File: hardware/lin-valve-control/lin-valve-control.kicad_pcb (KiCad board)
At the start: 4 copper layers, 55.6 x 43.2 mm, 46 parts, among them J1 UPDI, J2 I2C LCD, J3 Screw_Terminal_01x03, J4 Screw_Terminal_01x05, Q1 2N7002, Q2 2N7002, U1 TJA1021T, U2 ATtiny824-X, U3 Voltage Regulator, U4 MCP1754S-3302xCB, U5 TCA9534, U6 DRV8801PWP

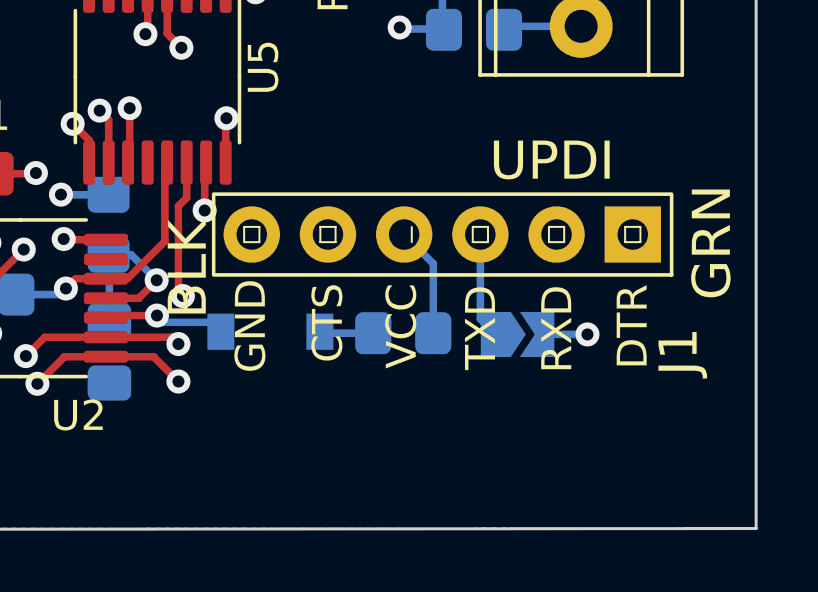
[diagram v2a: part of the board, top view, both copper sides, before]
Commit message: Update the schematics... remove PCA9536, use voltage regulator
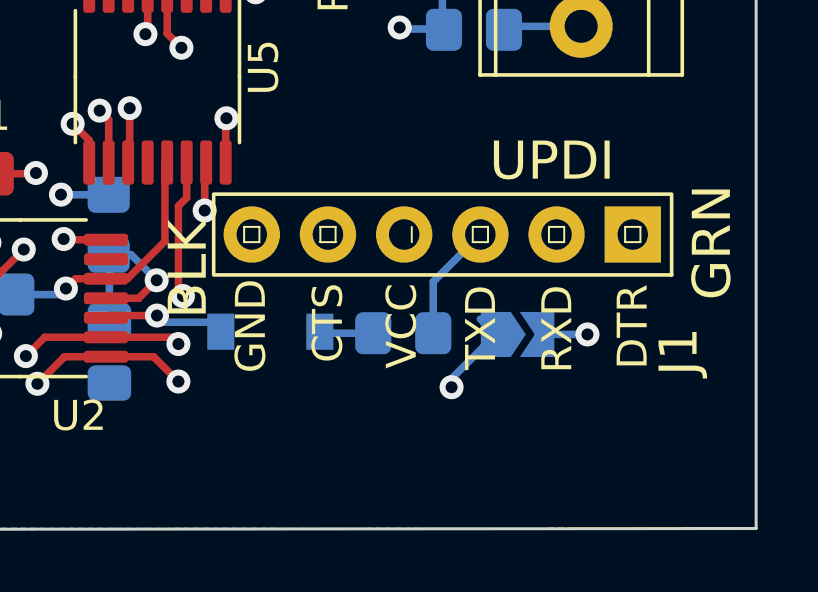
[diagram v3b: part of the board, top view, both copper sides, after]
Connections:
- J1 pad 1: GND -> unconnected-(J1-Pad1)
- J1 pad 2: unconnected-(J1-Pad2) -> UPDI
- J1 pad 4: Net-(J1-Pad4) -> Net-(JP1-Pad1)
- J1 pad 5: UPDI -> unconnected-(J1-Pad5)
- J1 pad 6: unconnected-(J1-Pad6) -> GND
- JP1 pad 1: Net-(J1-Pad3) -> Net-(JP1-Pad1)
- R6 pad 2: Net-(J1-Pad4) -> Net-(J1-Pad3)
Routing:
- net Net-(JP1-Pad1): track 0.00 -> 8.84 mm, vias 0 -> 1
- net UPDI: track 11.1 -> 18.7 mm
- net Net-(J1-Pad4): track 3.69 -> 0.00 mm
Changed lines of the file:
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@@
   (net 8 "SCL")
   (net 9 "SDA")
-  (net 10 "Net-(U2-Pad5)")
+  (net 10 "unconnected-(J1-Pad1)")
   (net 11 "unconnected-(U3-Pad4)")
   (net 12 "Net-(C10-Pad1)")
@@
   (net 18 "UPDI")
   (net 19 "+BATT")
-  (net 20 "unconnected-(J1-Pad2)")
+  (net 20 "Net-(JP1-Pad1)")
   (net 21 "Net-(J1-Pad3)")
   (net 22 "Net-(D2-Pad1)")
@@
   (net 25 "SCL5V")
   (net 26 "SDA5V")
-  (net 27 "Net-(J1-Pad4)")
-  (net 28 "unconnected-(J1-Pad6)")
+  (net 27 "unconnected-(J1-Pad5)")
+  (net 28 "Net-(R5-Pad1)")
   (net 29 "VALVE+")
   (net 30 "VALVE-")
@@
       (net 7 "~{LIN_WAKE}") (pinfunction "PA6") (pintype "bidirectional"))
     (pad "5" smd roundrect (at -2.8625 0.65) (size 1.475 0.4) (layers "F.Cu" "F.Paste" "F.Mask") (roundrect_rratio 0.25)
-      (net 10 "Net-(U2-Pad5)") (pinfunction "PA7") (pintype "bidirectional"))
+      (net 28 "Net-(R5-Pad1)") (pinfunction "PA7") (pintype "bidirectional"))
     (pad "6" smd roundrect (at -2.8625 1.3) (size 1.475 0.4) (layers "F.Cu" "F.Paste" "F.Mask") (roundrect_rratio 0.25)
       (net 5 "RXD") (pinfunction "PB3") (pintype "bidirectional"))
@@
     (fp_rect (start -1.2954 -1.3462) (end 13.97 1.3462) (layer "F.SilkS") (width 0.12) (fill none))
     (pad "1" thru_hole rect (at 0 0 180) (size 1.8796 1.8796) (drill 1.016) (layers *.Cu *.Paste *.Mask)
-      (net 1 "GND") (pinfunction "GND") (pintype "passive"))
+      (net 10 "unconnected-(J1-Pad1)") (pinfunction "DTR") (pintype "passive+no_connect"))
     (pad "2" thru_hole circle (at 2.54 0 180) (size 1.8796 1.8796) (drill 1.016) (layers *.Cu *.Paste *.Mask)
-      (net 20 "unconnected-(J1-Pad2)") (pinfunction "CTS") (pintype "passive+no_connect"))
+      (net 18 "UPDI") (pinfunction "RXD") (pintype "passive"))
     (pad "3" thru_hole circle (at 5.08 0 180) (size 1.8796 1.8796) (drill 1.016) (layers *.Cu *.Paste *.Mask)
-      (net 21 "Net-(J1-Pad3)") (pinfunction "VCC") (pintype "passive"))
+      (net 21 "Net-(J1-Pad3)") (pinfunction "TXD") (pintype "passive"))
     (pad "4" thru_hole circle (at 7.62 0 180) (size 1.8796 1.8796) (drill 1.016) (layers *.Cu *.Paste *.Mask)
-      (net 27 "Net-(J1-Pad4)") (pinfunction "TXD") (pintype "passive"))
+      (net 20 "Net-(JP1-Pad1)") (pinfunction "VCC") (pintype "passive"))
     (pad "5" thru_hole circle (at 10.16 0 180) (size 1.8796 1.8796) (drill 1.016) (layers *.Cu *.Paste *.Mask)
-      (net 18 "UPDI") (pinfunction "RXD") (pintype "passive"))
+      (net 27 "unconnected-(J1-Pad5)") (pinfunction "CTS") (pintype "passive+no_connect"))
     (pad "6" thru_hole circle (at 12.7 0 180) (size 1.8796 1.8796) (drill 1.016) (layers *.Cu *.Paste *.Mask)
-      (net 28 "unconnected-(J1-Pad6)") (pinfunction "RTS") (pintype "passive+no_connect"))
+      (net 1 "GND") (pinfunction "GND") (pintype "passive"))
   )
   (footprint "Package_SO:HTSSOP-16-1EP_4.4x5mm_P0.65mm_EP3.4x5mm_Mask3x3mm_ThermalVias" (layer "F.Cu")
@@
       (net 22 "Net-(D2-Pad1)") (pintype "passive"))
     (pad "2" smd roundrect (at 1 0) (size 1.2 1.4) (layers "B.Cu" "B.Paste" "B.Mask") (roundrect_rratio 0.2083333333)
-      (net 27 "Net-(J1-Pad4)") (pintype "passive"))
+      (net 21 "Net-(J1-Pad3)") (pintype "passive"))
     (model "${KICAD6_3DMODEL_DIR}/Resistor_SMD.3dshapes/R_0805_2012Metric.wrl"
       (offset (xyz 0 0 0))
@@
     (fp_line (start -1 0.625) (end 1 0.625) (layer "B.Fab") (width 0.1))
     (pad "1" smd roundrect (at -1 0 90) (size 1.2 1.4) (layers "B.Cu" "B.Paste" "B.Mask") (roundrect_rratio 0.2083333333)
-      (net 10 "Net-(U2-Pad5)") (pintype "passive"))
+      (net 28 "Net-(R5-Pad1)") (pintype "passive"))
     (pad "2" smd roundrect (at 1 0 90) (size 1.2 1.4) (layers "B.Cu" "B.Paste" "B.Mask") (roundrect_rratio 0.2083333333)
       (net 16 "Net-(D1-Pad2)") (pintype "passive"))
@@
     (fp_line (start -1.65 1.25) (end 1.65 1.25) (layer "B.CrtYd") (width 0.05))
     (pad "1" smd custom (at -0.725 0) (size 0.3 0.3) (layers "B.Cu" "B.Mask")
-      (net 21 "Net-(J1-Pad3)") (pinfunction "A") (pintype "passive") (zone_connect 2)
+      (net 20 "Net-(JP1-Pad1)") (pinfunction "A") (pintype "passive") (zone_connect 2)
       (options (clearance outline) (anchor rect))
       (primitives
@@
   (segment (start 184.3 88.45) (end 184.3 89.2) (width 0.25) (layer "B.Cu") (net 9))
   (segment (start 184.3 89.2) (end 185.425 90.325) (width 0.25) (layer "B.Cu") (net 9))
-  (segment (start 203.945 94.575) (end 206.22 92.3) (width 0.25) (layer "F.Cu") (net 10))
-  (segment (start 203.2375 94.575) (end 203.945 94.575) (width 0.25) (layer "F.Cu") (net 10))
-  (via (at 203.735286 87.711025) (size 0.8) (drill 0.4) (layers "F.Cu" "B.Cu") (net 10))
-  (via (at 206.22 92.3) (size 0.8) (drill 0.4) (layers "F.Cu" "B.Cu") (net 10))
-  (segment (start 205.9 89.96) (end 203.68 87.74) (width 0.25) (layer "In1.Cu") (net 10))
-  (segment (start 205.9 91.98) (end 205.9 89.96) (width 0.25) (layer "In1.Cu") (net 10))
-  (segment (start 206.22 92.3) (end 205.9 91.98) (width 0.25) (layer "In1.Cu") (net 10))
-  (segment (start 203.708975 87.711025) (end 203.735286 87.711025) (width 0.25) (layer "In1.Cu") (net 10))
-  (segment (start 203.68 87.74) (end 203.708975 87.711025) (width 0.25) (layer "In1.Cu") (net 10))
-  (segment (start 202.72 86.695739) (end 203.735286 87.711025) (width 0.25) (layer "B.Cu") (net 10))
-  (segment (start 202.72 86.37) (end 202.72 86.695739) (width 0.25) (layer "B.Cu") (net 10))
   (segment (start 213.375 72.6) (end 214.05 71.925) (width 0.25) (layer "F.Cu") (net 12))
   (segment (start 214.05 71.925) (end 215.125 71.925) (width 0.25) (layer "F.Cu") (net 12))
@@
   (segment (start 211.5125 63.91) (end 211.42 63.8175) (width 0.25) (layer "F.Cu") (net 17))
   (segment (start 209.037 94.5005) (end 208.9625 94.575) (width 0.25) (layer "F.Cu") (net 18))
-  (segment (start 216.4 91.84) (end 216.36 91.8) (width 0.25) (layer "F.Cu") (net 18))
   (segment (start 210.66 94.5005) (end 209.037 94.5005) (width 0.25) (layer "F.Cu") (net 18))
   (via (at 210.66 94.5005) (size 0.8) (drill 0.4) (layers "F.Cu" "B.Cu") (net 18))
-  (segment (start 216.36 91.8) (end 213.435 94.725) (width 0.25) (layer "In2.Cu") (net 18))
-  (segment (start 213.435 94.725) (end 210.8845 94.725) (width 0.25) (layer "In2.Cu") (net 18))
   (segment (start 210.8845 94.725) (end 210.66 94.5005) (width 0.25) (layer "In2.Cu") (net 18))
+  (segment (start 221.055 94.725) (end 210.8845 94.725) (width 0.25) (layer "In2.Cu") (net 18))
+  (segment (start 223.98 91.8) (end 221.055 94.725) (width 0.25) (layer "In2.Cu") (net 18))
   (segment (start 212.79 95.04) (end 212.475 94.725) (width 0.25) (layer "B.Cu") (net 18))
   (segment (start 212.475 94.725) (end 210.8845 94.725) (width 0.25) (layer "B.Cu") (net 18))
@@
   (segment (start 224.7 64) (end 219.32 64) (width 1.2) (layer "F.Cu") (net 19))
   (segment (start 219.32 64) (end 219.23 63.91) (width 0.25) (layer "F.Cu") (net 19))
-  (segment (start 221.44 91.8) (end 221.44 94.615) (width 0.25) (layer "B.Cu") (net 21))
-  (segment (start 221.44 94.615) (end 221.955 95.13) (width 0.25) (layer "B.Cu") (net 21))
+  (via (at 220.48 96.89) (size 0.8) (drill 0.4) (layers "F.Cu" "B.Cu") (net 20))
+  (segment (start 218.9 91.8) (end 218.9 95.31) (width 0.25) (layer "In1.Cu") (net 20))
+  (segment (start 218.9 95.31) (end 220.48 96.89) (width 0.25) (layer "In1.Cu") (net 20))
+  (segment (start 220.48 96.89) (end 220.48 96.605) (width 0.25) (layer "B.Cu") (net 20))
+  (segment (start 221.44 94.615) (end 221.955 95.13) (width 0.25) (layer "B.Cu") (net 20))
+  (segment (start 220.48 96.605) (end 221.955 95.13) (width 0.25) (layer "B.Cu") (net 20))
+  (segment (start 219.87 95.09) (end 219.87 93.37) (width 0.25) (layer "B.Cu") (net 21))
+  (segment (start 219.87 93.37) (end 221.44 91.8) (width 0.25) (layer "B.Cu") (net 21))
   (segment (start 217.87 95.09) (end 216.14 95.09) (width 0.25) (layer "B.Cu") (net 22))
   (segment (start 216.14 95.09) (end 216.09 95.04) (width 0.25) (layer "B.Cu") (net 22))
@@
   (segment (start 184.4 84.725) (end 184.4 82.93) (width 0.25) (layer "B.Cu") (net 26))
   (segment (start 184.4 82.93) (end 185.23 82.1) (width 0.25) (layer "B.Cu") (net 26))
-  (segment (start 218.9 91.8) (end 219.87 92.77) (width 0.25) (layer "B.Cu") (net 27))
-  (segment (start 219.87 92.77) (end 219.87 95.09) (width 0.25) (layer "B.Cu") (net 27))
+  (segment (start 216.4 91.84) (end 216.36 91.8) (width 0.25) (layer "F.Cu") (net 27))
+  (segment (start 203.945 94.575) (end 206.22 92.3) (width 0.25) (layer "F.Cu") (net 28))
+  (segment (start 203.2375 94.575) (end 203.945 94.575) (width 0.25) (layer "F.Cu") (net 28))
+  (via (at 203.735286 87.711025) (size 0.8) (drill 0.4) (layers "F.Cu" "B.Cu") (net 28))
+  (via (at 206.22 92.3) (size 0.8) (drill 0.4) (layers "F.Cu" "B.Cu") (net 28))
+  (segment (start 205.9 89.96) (end 203.68 87.74) (width 0.25) (layer "In1.Cu") (net 28))
+  (segment (start 205.9 91.98) (end 205.9 89.96) (width 0.25) (layer "In1.Cu") (net 28))
+  (segment (start 206.22 92.3) (end 205.9 91.98) (width 0.25) (layer "In1.Cu") (net 28))
+  (segment (start 203.708975 87.711025) (end 203.735286 87.711025) (width 0.25) (layer "In1.Cu") (net 28))
+  (segment (start 203.68 87.74) (end 203.708975 87.711025) (width 0.25) (layer "In1.Cu") (net 28))
+  (segment (start 202.72 86.695739) (end 203.735286 87.711025) (width 0.25) (layer "B.Cu") (net 28))
+  (segment (start 202.72 86.37) (end 202.72 86.695739) (width 0.25) (layer "B.Cu") (net 28))
   (segment (start 214.025 81.975) (end 214.575 82.525) (width 0.2) (layer "F.Cu") (net 29))
   (segment (start 214.025 80.675) (end 214.025 81.975) (width 0.2) (layer "F.Cu") (net 29))
